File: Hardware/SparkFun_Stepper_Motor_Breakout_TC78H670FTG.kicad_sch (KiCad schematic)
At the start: 24 parts, among them J1 Conn_01x08, J2 Conn_01x08, U1 TC78H670FTG

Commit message: changing file names to "breakout"
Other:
- title: SparkFun Stepper Motor Carrier TC78H670FTG -> SparkFun Stepper Motor Breakout TC78H670FTG

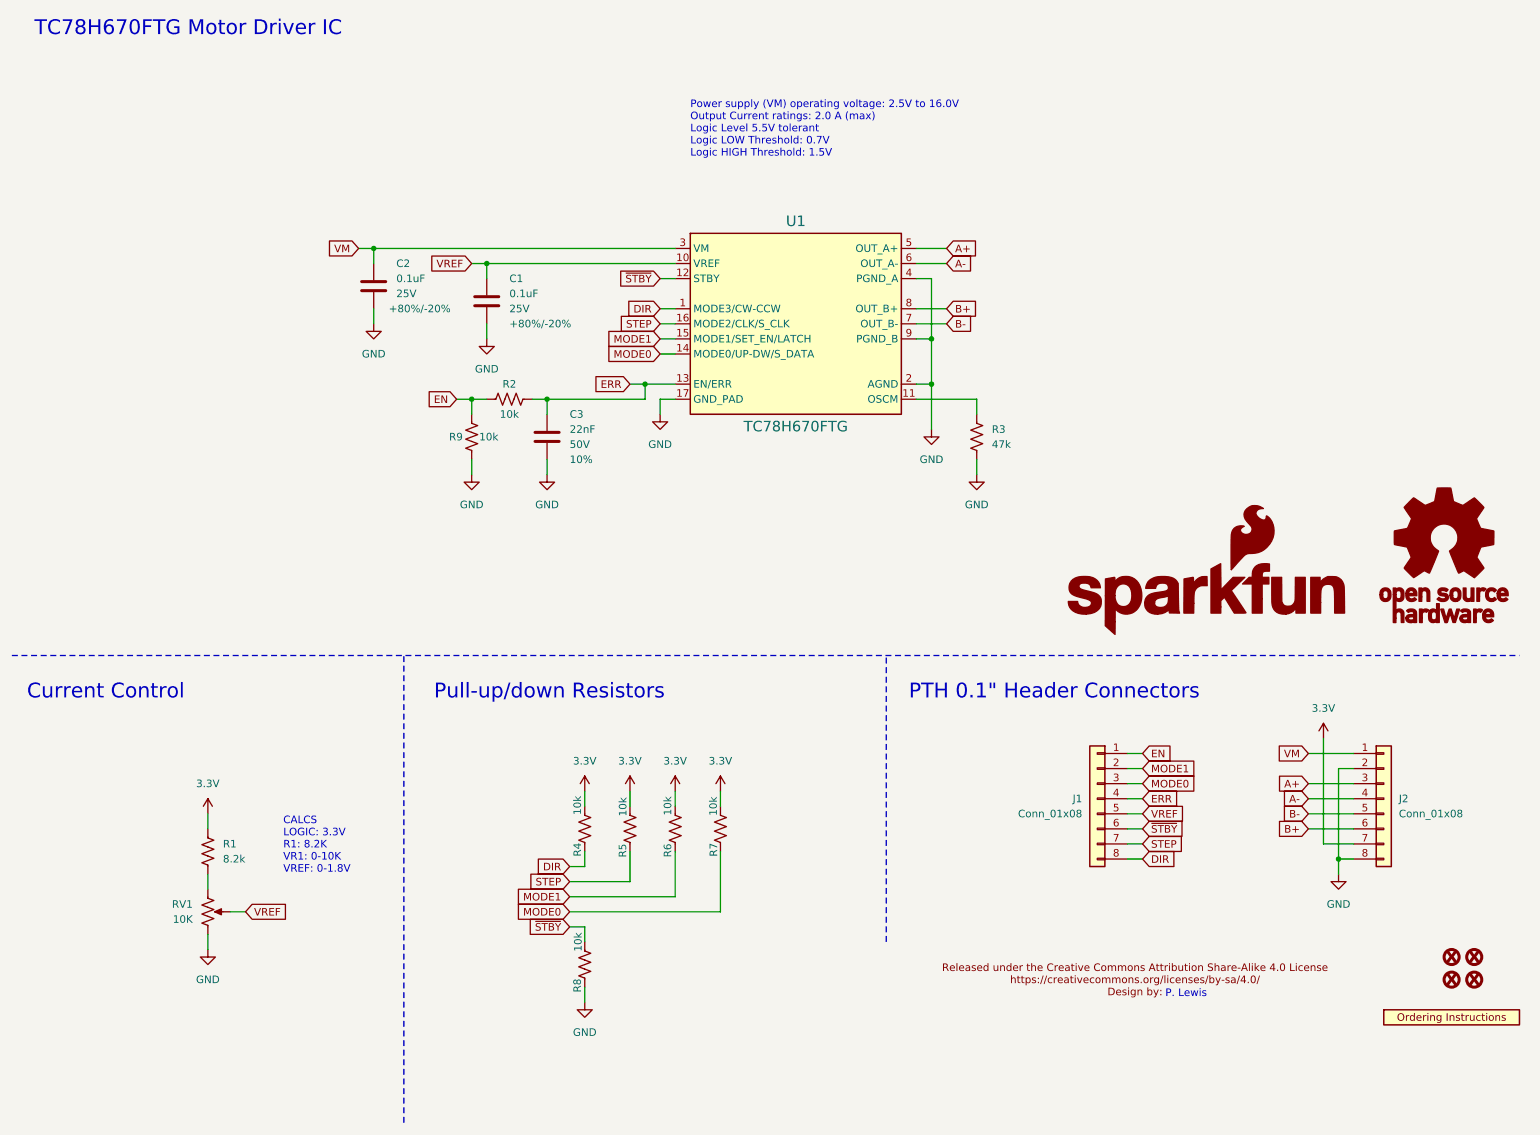
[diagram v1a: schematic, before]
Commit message: updated trimpot
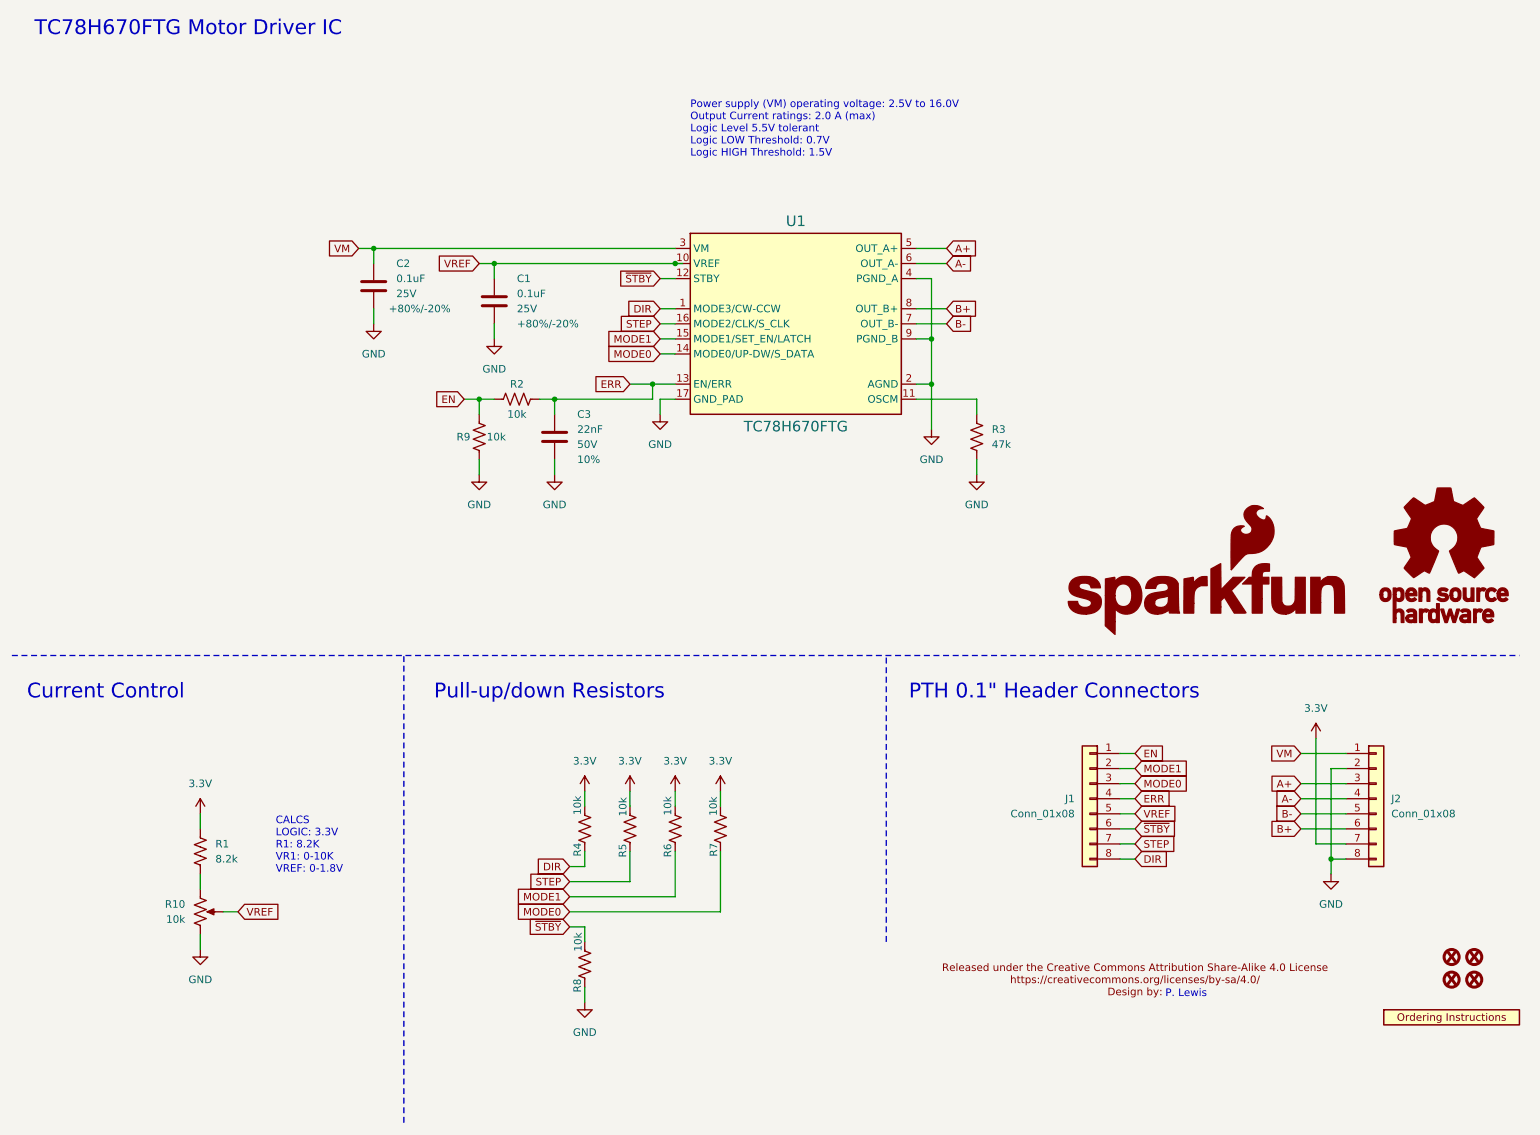
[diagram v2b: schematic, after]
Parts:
- R10: renamed from RV1; value 10K -> 10k; symbol SparkFun-Resistor:R_Trimpot_SMD_3MM_Closed -> SparkFun-Resistor:Trimpot_10k_SMD_3.0x3.0mm
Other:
- moved on the sheet: C1, C3, J1, J2, R1, R10, R2, R9

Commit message: corrected motor driver IC footprint
I had the pins numbered incorrectly, had to re-route most things.
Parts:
- removed R8: 10k, SparkFun-Resistor:R_0603_1608Metric, symbol SparkFun-Resistor:10k_0603
- J1: footprint SparkFun-Connector:1X08 -> SparkFun-Connector:1x08
- U2: footprint SparkFun-Aesthetic:ORDERING_INSTRUCTIONS -> SparkFun-Aesthetic:Ordering_Instructions
- renumbered C2 to C1, C1 to C2, FID3 to FID2, FID2 to FID3, G2 to G1, G1 to G2, R3 to R10, R10 to R2, R9 to R3, R2 to R4, R4 to R5, R5 to R7, R6 to R8, R7 to R9
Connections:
- net A+: now also J2.6 (Pin_6); no longer J2.3 (Pin_3)
- net A-: now also J2.5 (Pin_5); no longer J2.4 (Pin_4)
- net B+: now also J2.3 (Pin_3); no longer J2.6 (Pin_6)
- net B-: now also J2.4 (Pin_4); no longer J2.5 (Pin_5)

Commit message: library work and sch cleanup
-moved to a 0.05" grid for schematic and tightened things up (made all nets shorter to match smaller grid and only use a single grid space to extend out from any pin)
-updated ordering instructions fp to avoid sch->brd update error
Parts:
- R2: footprint SparkFun-Resistor:TRIMPOT-SMD-3MM-CLOSED -> SparkFun-Resistor:Trimpot_SMD_3.0x3.0mm; Mfg Part# (none) -> 22AR10K
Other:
- moved on the sheet: C1, C2, C3, J1, J2, R1, R10, R3, R4, R5, R7, R8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
